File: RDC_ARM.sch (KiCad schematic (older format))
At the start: 32 parts, among them J1 CN_ARM, Q1 BC807, Q2 BC807, U2 AD8397ARZ, X1 8.192MHz

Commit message: cambios en el placement
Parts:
- renumbered C11 to C1, C8 to C10, C15 to C11, C9 to C12, C10 to C13, C12 to C2, C14 to C3, C3 to C4, C6 to C5, C4 to C6, C13 to C8, C5 to C9, R12 to R1, R11 to R10, R13 to R11, R4 to R2, R6 to R3, R8 to R4, R9 to R5, R3 to R6, R1 to R7, R7 to R8, R10 to R9, U2 to U1

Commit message: routeado completo, quedan 32 vias
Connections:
- wire segments 129 -> 131
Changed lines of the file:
@@
 Wire Wire Line
 	7900 4250 7600 4250
-Text Label 10400 4350 2    60   ~ 0
+Text Label 10500 3250 2    60   ~ 0
 COS
-Text Label 10400 4450 2    60   ~ 0
+Text Label 10500 3350 2    60   ~ 0
 COSLO
-Text Label 10400 4150 2    60   ~ 0
+Text Label 10500 3650 2    60   ~ 0
 SINLO
-Text Label 10400 4050 2    60   ~ 0
+Text Label 10500 3550 2    60   ~ 0
 SIN
 Wire Wire Line
-	10500 4450 10100 4450
-Wire Wire Line
-	10500 4350 10100 4350
-Wire Wire Line
-	10500 4150 10100 4150
-Wire Wire Line
-	10500 4050 10100 4050
-Text Label 10400 4550 2    60   ~ 0
+	10600 3350 10200 3350
+Wire Wire Line
+	10600 3250 10200 3250
+Wire Wire Line
+	10600 3650 10200 3650
+Wire Wire Line
+	10600 3550 10200 3550
+Text Label 10500 4050 2    60   ~ 0
 AGND
-Text Label 10400 4250 2    60   ~ 0
+Text Label 10500 3750 2    60   ~ 0
 AGND
-Text Label 10400 3950 2    60   ~ 0
+Text Label 10500 3450 2    60   ~ 0
 AGND
 Wire Wire Line
-	10500 4550 10100 4550
-Wire Wire Line
-	10500 4250 10100 4250
-Wire Wire Line
-	10500 3950 10100 3950
-Wire Wire Line
-	9950 3850 10500 3850
-Wire Wire Line
-	9950 3750 10500 3750
+	10600 4050 10200 4050
+Wire Wire Line
+	10600 3750 10200 3750
+Wire Wire Line
+	10600 3450 10200 3450
+Wire Wire Line
+	10050 3950 10600 3950
 $Comp
 L Connector:Screw_Terminal_01x09 J?
 U 1 1 5EFA861B
-P 10700 4150
+P 10800 3650
 AR Path="/5EFA861B" Ref="J?"  Part="1"
 AR Path="/5EF45E27/5EFA861B" Ref="J1"  Part="1"
 AR Path="/5F077C82/5EFA861B" Ref="J?"  Part="1"
-F 0 "J1" H 10780 4192 50  0000 L CNN
-F 1 "CN_ARM" H 10780 4101 50  0000 L CNN
-F 2 "TerminalBlock_Phoenix:TerminalBlock_Phoenix_MKDS-1,5-9-5.08_1x09_P5.08mm_Horizontal" H 10700 4150 50  0001 C CNN
-F 3 "~" H 10700 4150 50  0001 C CNN
-	1    10700 4150
+F 0 "J1" H 10880 3692 50  0000 L CNN
+F 1 "CN_ARM" H 10880 3601 50  0000 L CNN
+F 2 "TerminalBlock_Phoenix:TerminalBlock_Phoenix_MKDS-1,5-9-5.08_1x09_P5.08mm_Horizontal" H 10800 3650 50  0001 C CNN
+F 3 "~" H 10800 3650 50  0001 C CNN
+	1    10800 3650
 	1    0    0    -1
 $EndComp
@@
 	9950 5100 9950 5450
 Wire Wire Line
-	9950 2950 9950 3300
-Wire Wire Line
 	9300 3300 9500 3300
 Wire Wire Line
@@
 Wire Wire Line
 	5800 2900 5800 2950
+Wire Wire Line
+	9950 2950 9950 3300
+Wire Wire Line
+	9950 3850 10600 3850
+Connection ~ 9950 3850
+Wire Wire Line
+	10050 3950 10050 3750
+Wire Wire Line
+	10050 3750 9950 3750
+Connection ~ 9950 3750
 $EndSCHEMATC

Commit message: cambiados conectores, agregado conversor 3,3->TTL drivers
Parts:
- removed J1: CN_ARM, TerminalBlock_Phoenix:TerminalBlock_Phoenix_MKDS-1,5-9-5.08_1x09_P5.08mm_Horizontal, symbol Connector:Screw_Terminal_01x09
- added J1: COS, Connector_JST:JST_EH_S3B-EH_1x03_P2.50mm_Horizontal, symbol Connector_Generic:Conn_01x03
- added J2: SIN, Connector_JST:JST_EH_S3B-EH_1x03_P2.50mm_Horizontal, symbol Connector_Generic:Conn_01x03
- added J3: EXC, Connector_JST:JST_EH_S3B-EH_1x03_P2.50mm_Horizontal, symbol Connector_Generic:Conn_01x03
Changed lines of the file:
@@
 $Descr A4 11693 8268
 encoding utf-8
-Sheet 3 5
+Sheet 3 6
 Title ""
 Date ""
@@
 Wire Wire Line
 	7900 4250 7600 4250
-Text Label 10500 3250 2    60   ~ 0
+Text Label 10500 2950 2    60   ~ 0
 COS
-Text Label 10500 3350 2    60   ~ 0
+Text Label 10500 3050 2    60   ~ 0
 COSLO
-Text Label 10500 3650 2    60   ~ 0
+Text Label 10500 3500 2    60   ~ 0
 SINLO
-Text Label 10500 3550 2    60   ~ 0
+Text Label 10500 3400 2    60   ~ 0
 SIN
 Wire Wire Line
-	10600 3350 10200 3350
-Wire Wire Line
-	10600 3250 10200 3250
-Wire Wire Line
-	10600 3650 10200 3650
-Wire Wire Line
-	10600 3550 10200 3550
+	10600 3050 10200 3050
+Wire Wire Line
+	10600 2950 10200 2950
+Wire Wire Line
+	10600 3500 10200 3500
+Wire Wire Line
+	10600 3400 10200 3400
 Text Label 10500 4050 2    60   ~ 0
 AGND
-Text Label 10500 3750 2    60   ~ 0
+Text Label 10500 3600 2    60   ~ 0
 AGND
-Text Label 10500 3450 2    60   ~ 0
+Text Label 10500 3150 2    60   ~ 0
 AGND
 Wire Wire Line
 	10600 4050 10200 4050
 Wire Wire Line
-	10600 3750 10200 3750
-Wire Wire Line
-	10600 3450 10200 3450
+	10600 3600 10200 3600
+Wire Wire Line
+	10600 3150 10200 3150
 Wire Wire Line
 	10050 3950 10600 3950
-$Comp
-L Connector:Screw_Terminal_01x09 J?
-U 1 1 5EFA861B
-P 10800 3650
-AR Path="/5EFA861B" Ref="J?"  Part="1"
-AR Path="/5EF45E27/5EFA861B" Ref="J1"  Part="1"
-AR Path="/5F077C82/5EFA861B" Ref="J?"  Part="1"
-F 0 "J1" H 10880 3692 50  0000 L CNN
-F 1 "CN_ARM" H 10880 3601 50  0000 L CNN
-F 2 "TerminalBlock_Phoenix:TerminalBlock_Phoenix_MKDS-1,5-9-5.08_1x09_P5.08mm_Horizontal" H 10800 3650 50  0001 C CNN
-F 3 "~" H 10800 3650 50  0001 C CNN
-	1    10800 3650
-	1    0    0    -1
-$EndComp
 $Comp
 L power:+12V #PWR?
@@
 	10050 3750 9950 3750
 Connection ~ 9950 3750
+$Comp
+L Connector_Generic:Conn_01x03 J1
+U 1 1 5F0B1A7A
+P 10800 3050
+F 0 "J1" H 10880 3092 50  0000 L CNN
+F 1 "COS" H 10880 3001 50  0000 L CNN
+F 2 "Connector_JST:JST_EH_S3B-EH_1x03_P2.50mm_Horizontal" H 10800 3050 50  0001 C CNN
+F 3 "~" H 10800 3050 50  0001 C CNN
+	1    10800 3050
+	1    0    0    -1
+$EndComp
+$Comp
+L Connector_Generic:Conn_01x03 J2
+U 1 1 5F0B3E39
+P 10800 3500
+F 0 "J2" H 10880 3542 50  0000 L CNN
+F 1 "SIN" H 10880 3451 50  0000 L CNN
+F 2 "Connector_JST:JST_EH_S3B-EH_1x03_P2.50mm_Horizontal" H 10800 3500 50  0001 C CNN
+F 3 "~" H 10800 3500 50  0001 C CNN
+	1    10800 3500
+	1    0    0    -1
+$EndComp
+$Comp
+L Connector_Generic:Conn_01x03 J3
+U 1 1 5F0B43E4
+P 10800 3950
+F 0 "J3" H 10880 3992 50  0000 L CNN
+F 1 "EXC" H 10880 3901 50  0000 L CNN
+F 2 "Connector_JST:JST_EH_S3B-EH_1x03_P2.50mm_Horizontal" H 10800 3950 50  0001 C CNN
+F 3 "~" H 10800 3950 50  0001 C CNN
+	1    10800 3950
+	1    0    0    -1
+$EndComp
 $EndSCHEMATC

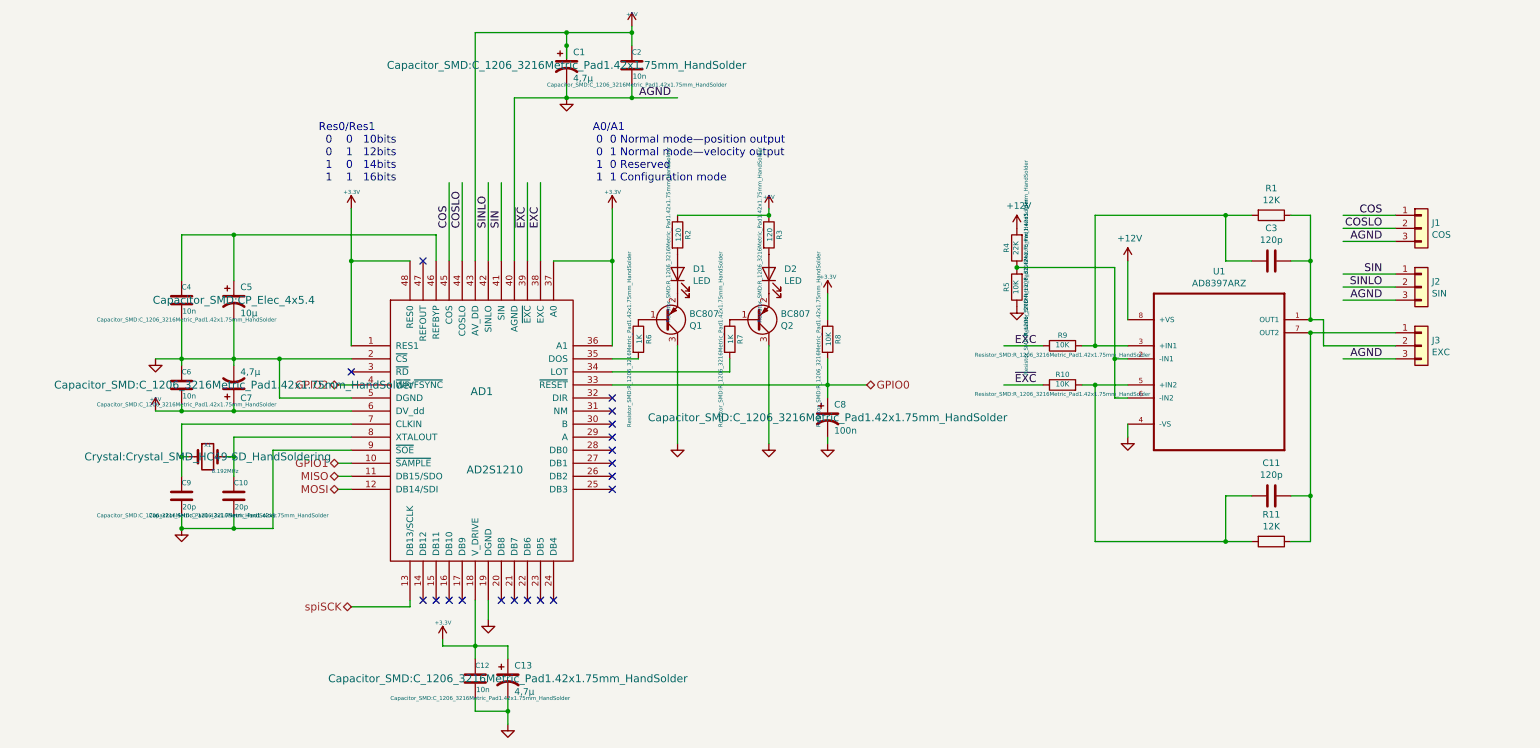
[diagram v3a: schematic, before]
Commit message: cambiado a conectores MOLEX KK, agregados test points para señales analogicas
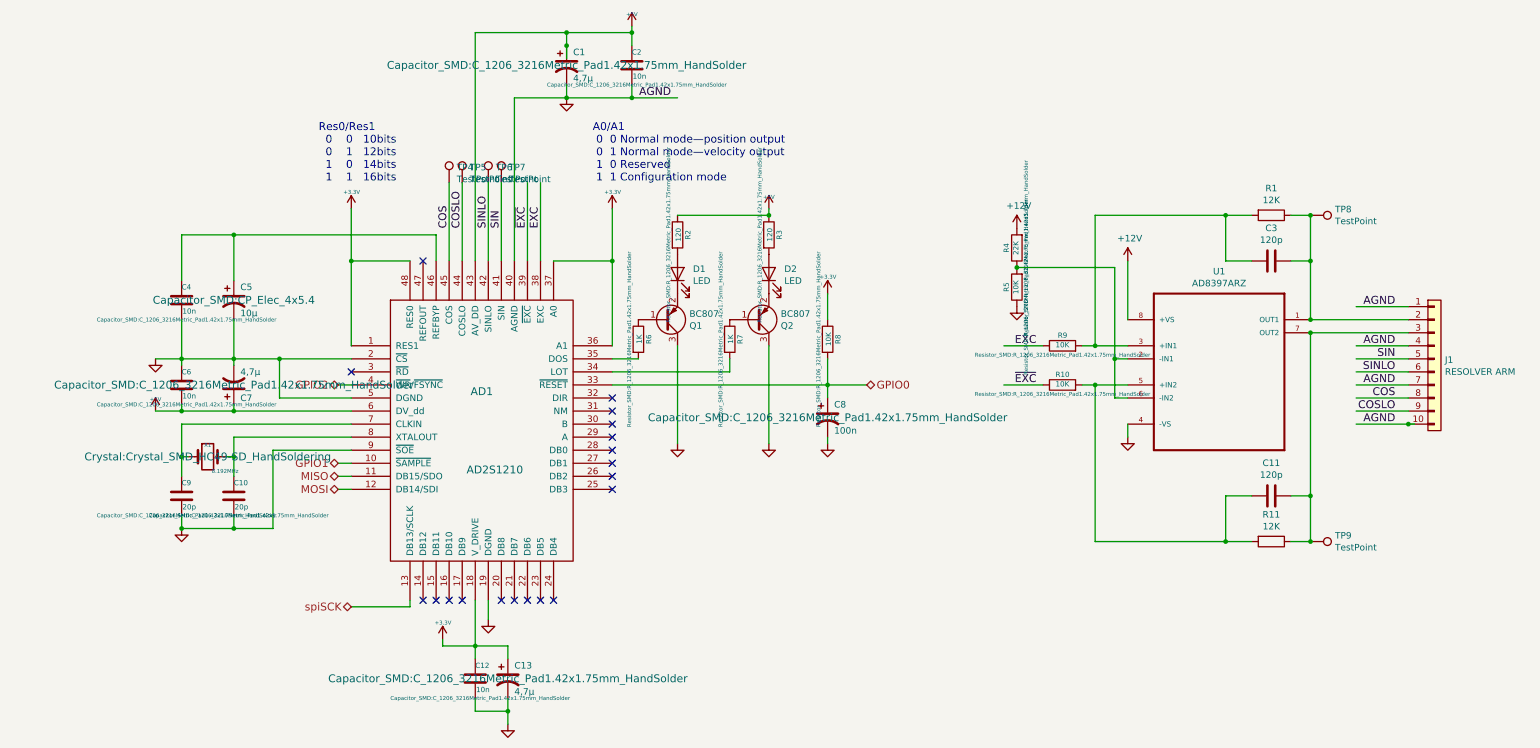
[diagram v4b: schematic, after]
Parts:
- removed J1: COS, Connector_JST:JST_EH_S3B-EH_1x03_P2.50mm_Horizontal, symbol Connector_Generic:Conn_01x03
- removed J2: SIN, Connector_JST:JST_EH_S3B-EH_1x03_P2.50mm_Horizontal, symbol Connector_Generic:Conn_01x03
- removed J3: EXC, Connector_JST:JST_EH_S3B-EH_1x03_P2.50mm_Horizontal, symbol Connector_Generic:Conn_01x03
- added J1: RESOLVER ARM, Connector_Molex:Molex_KK-254_AE-6410-10A_1x10_P2.54mm_Vertical, symbol Connector_Generic:Conn_01x10
- added TP4, TP5, TP6, TP7, TP8, TP9: TestPoint, TestPoint:TestPoint_THTPad_1.0x1.0mm_Drill0.5mm, symbol Connector:TestPoint
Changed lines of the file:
@@
 Wire Wire Line
 	7900 4250 7600 4250
-Text Label 10500 2950 2    60   ~ 0
+Text Label 10600 4350 2    60   ~ 0
 COS
-Text Label 10500 3050 2    60   ~ 0
+Text Label 10600 4450 2    60   ~ 0
 COSLO
-Text Label 10500 3500 2    60   ~ 0
+Text Label 10600 4150 2    60   ~ 0
 SINLO
-Text Label 10500 3400 2    60   ~ 0
+Text Label 10600 4050 2    60   ~ 0
 SIN
 Wire Wire Line
-	10600 3050 10200 3050
-Wire Wire Line
-	10600 2950 10200 2950
-Wire Wire Line
-	10600 3500 10200 3500
-Wire Wire Line
-	10600 3400 10200 3400
-Text Label 10500 4050 2    60   ~ 0
+	10700 4450 10300 4450
+Wire Wire Line
+	10700 4350 10300 4350
+Wire Wire Line
+	10700 4150 10300 4150
+Wire Wire Line
+	10700 4050 10300 4050
+Text Label 10600 4250 2    60   ~ 0
 AGND
-Text Label 10500 3600 2    60   ~ 0
+Text Label 10600 3950 2    60   ~ 0
 AGND
-Text Label 10500 3150 2    60   ~ 0
-AGND
-Wire Wire Line
-	10600 4050 10200 4050
-Wire Wire Line
-	10600 3600 10200 3600
-Wire Wire Line
-	10600 3150 10200 3150
-Wire Wire Line
-	10050 3950 10600 3950
+Wire Wire Line
+	10700 4250 10300 4250
+Wire Wire Line
+	10700 3950 10300 3950
 $Comp
 L power:+12V #PWR?
@@
 Wire Wire Line
 	9950 2950 9950 3300
-Wire Wire Line
-	9950 3850 10600 3850
+$Comp
+L Connector_Generic:Conn_01x10 J1
+U 1 1 5F06A12E
+P 10900 4050
+F 0 "J1" H 10980 4042 50  0000 L CNN
+F 1 "RESOLVER ARM" H 10980 3951 50  0000 L CNN
+F 2 "Connector_Molex:Molex_KK-254_AE-6410-10A_1x10_P2.54mm_Vertical" H 10900 4050 50  0001 C CNN
+F 3 "~" H 10900 4050 50  0001 C CNN
+	1    10900 4050
+	1    0    0    -1
+$EndComp
+Wire Wire Line
+	10750 4550 10700 4550
+$Comp
+L Connector:TestPoint TP4
+U 1 1 5F0A4859
+P 3350 2700
+F 0 "TP4" H 3408 2818 50  0000 L CNN
+F 1 "TestPoint" H 3408 2727 50  0000 L CNN
+F 2 "TestPoint:TestPoint_THTPad_1.0x1.0mm_Drill0.5mm" H 3550 2700 50  0001 C CNN
+F 3 "~" H 3550 2700 50  0001 C CNN
+	1    3350 2700
+	1    0    0    -1
+$EndComp
+$Comp
+L Connector:TestPoint TP5
+U 1 1 5F0A6B93
+P 3450 2700
+F 0 "TP5" H 3508 2818 50  0000 L CNN
+F 1 "TestPoint" H 3508 2727 50  0000 L CNN
+F 2 "TestPoint:TestPoint_THTPad_1.0x1.0mm_Drill0.5mm" H 3650 2700 50  0001 C CNN
+F 3 "~" H 3650 2700 50  0001 C CNN
+	1    3450 2700
+	1    0    0    -1
+$EndComp
+$Comp
+L Connector:TestPoint TP6
+U 1 1 5F0A729F
+P 3650 2700
+F 0 "TP6" H 3708 2818 50  0000 L CNN
+F 1 "TestPoint" H 3708 2727 50  0000 L CNN
+F 2 "TestPoint:TestPoint_THTPad_1.0x1.0mm_Drill0.5mm" H 3850 2700 50  0001 C CNN
+F 3 "~" H 3850 2700 50  0001 C CNN
+	1    3650 2700
+	1    0    0    -1
+$EndComp
+$Comp
+L Connector:TestPoint TP7
+U 1 1 5F0A7B14
+P 3750 2700
+F 0 "TP7" H 3808 2818 50  0000 L CNN
+F 1 "TestPoint" H 3808 2727 50  0000 L CNN
+F 2 "TestPoint:TestPoint_THTPad_1.0x1.0mm_Drill0.5mm" H 3950 2700 50  0001 C CNN
+F 3 "~" H 3950 2700 50  0001 C CNN
+	1    3750 2700
+	1    0    0    -1
+$EndComp
+$Comp
+L Connector:TestPoint TP8
+U 1 1 5F0A9078
+P 9950 2950
+F 0 "TP8" V 9904 3138 50  0000 L CNN
+F 1 "TestPoint" V 9995 3138 50  0000 L CNN
+F 2 "TestPoint:TestPoint_THTPad_1.0x1.0mm_Drill0.5mm" H 10150 2950 50  0001 C CNN
+F 3 "~" H 10150 2950 50  0001 C CNN
+	1    9950 2950
+	0    1    1    0
+$EndComp
+Connection ~ 9950 2950
+$Comp
+L Connector:TestPoint TP9
+U 1 1 5F0A9A85
+P 9950 5450
+F 0 "TP9" V 9904 5638 50  0000 L CNN
+F 1 "TestPoint" V 9995 5638 50  0000 L CNN
+F 2 "TestPoint:TestPoint_THTPad_1.0x1.0mm_Drill0.5mm" H 10150 5450 50  0001 C CNN
+F 3 "~" H 10150 5450 50  0001 C CNN
+	1    9950 5450
+	0    1    1    0
+$EndComp
+Connection ~ 9950 5450
+Wire Wire Line
+	10700 4550 10300 4550
+Text Label 10600 4550 2    60   ~ 0
+AGND
+Connection ~ 10700 4550
+Wire Wire Line
+	9950 3750 10700 3750
+Connection ~ 9950 3750
+Wire Wire Line
+	9950 3850 10700 3850
 Connection ~ 9950 3850
 Wire Wire Line
-	10050 3950 10050 3750
-Wire Wire Line
-	10050 3750 9950 3750
-Connection ~ 9950 3750
-$Comp
-L Connector_Generic:Conn_01x03 J1
-U 1 1 5F0B1A7A
-P 10800 3050
-F 0 "J1" H 10880 3092 50  0000 L CNN
-F 1 "COS" H 10880 3001 50  0000 L CNN
-F 2 "Connector_JST:JST_EH_S3B-EH_1x03_P2.50mm_Horizontal" H 10800 3050 50  0001 C CNN
-F 3 "~" H 10800 3050 50  0001 C CNN
-	1    10800 3050
-	1    0    0    -1
-$EndComp
-$Comp
-L Connector_Generic:Conn_01x03 J2
-U 1 1 5F0B3E39
-P 10800 3500
-F 0 "J2" H 10880 3542 50  0000 L CNN
-F 1 "SIN" H 10880 3451 50  0000 L CNN
-F 2 "Connector_JST:JST_EH_S3B-EH_1x03_P2.50mm_Horizontal" H 10800 3500 50  0001 C CNN
-F 3 "~" H 10800 3500 50  0001 C CNN
-	1    10800 3500
-	1    0    0    -1
-$EndComp
-$Comp
-L Connector_Generic:Conn_01x03 J3
-U 1 1 5F0B43E4
-P 10800 3950
-F 0 "J3" H 10880 3992 50  0000 L CNN
-F 1 "EXC" H 10880 3901 50  0000 L CNN
-F 2 "Connector_JST:JST_EH_S3B-EH_1x03_P2.50mm_Horizontal" H 10800 3950 50  0001 C CNN
-F 3 "~" H 10800 3950 50  0001 C CNN
-	1    10800 3950
-	1    0    0    -1
-$EndComp
+	10700 3650 10300 3650
+Text Label 10600 3650 2    60   ~ 0
+AGND
 $EndSCHEMATC
